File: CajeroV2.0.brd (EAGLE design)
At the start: 105 x 69 mm, 45 parts, among them K2 G5LE, T2 2N2222, T3 2N3904

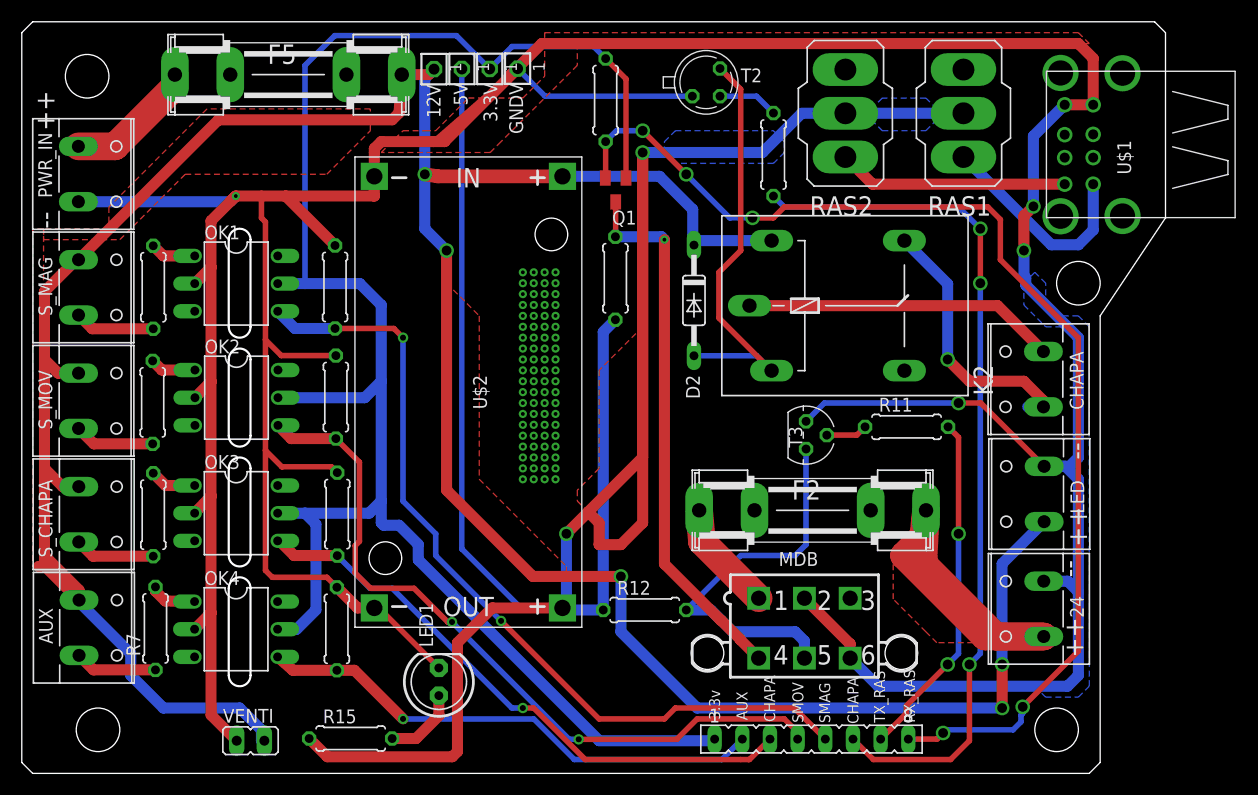
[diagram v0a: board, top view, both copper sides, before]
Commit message: V2.1
Cambio de posición un fusible y arreglo overlap
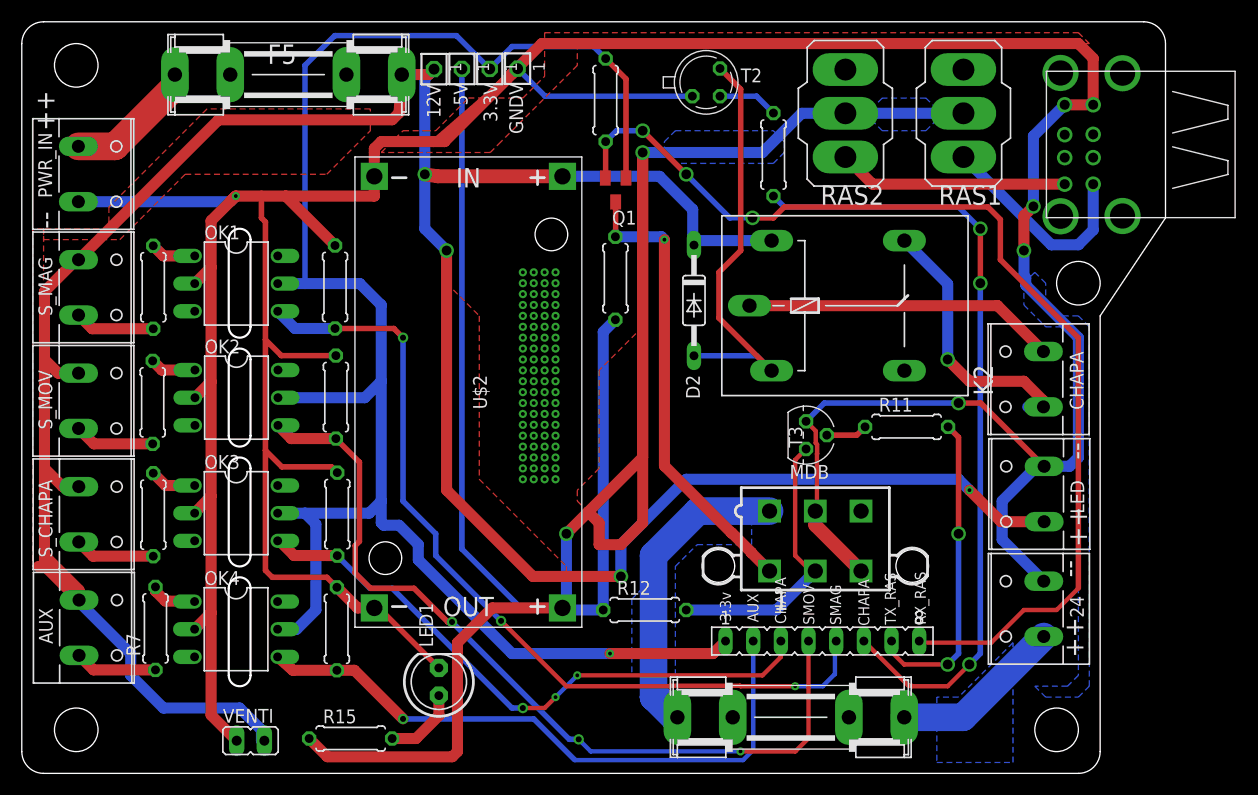
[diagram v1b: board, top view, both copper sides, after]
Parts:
- moved F2 19.1 mm to (70.6, 5.15)
- moved SV2 9.06 mm to (73.5, 12.1)
- moved MDB 8.06 mm to (72.8, 21.3)
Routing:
- net GND: track 397.3 -> 371.1 mm
- net 24VDC: track 39.5 -> 15.9 mm
- net N$21: track 10.2 -> 31.1 mm
- net +12V: track 275.6 -> 259.8 mm, vias 5 -> 4
- net ENTRADA_AUX: track 47.3 -> 57.9 mm
- net MASTER_TRANSMIT: track 35.9 -> 26.0 mm
- net SENSORMOV: track 68.1 -> 77.0 mm, vias 2 -> 3
- net RX_RASPBERRY: track 106.5 -> 97.8 mm, vias 5 -> 3
- net MASTER_RECEIVE: track 49.8 -> 42.3 mm
- net CHAPA: track 79.8 -> 72.9 mm
- net TX_RASPBERRY: track 32.0 -> 29.3 mm
- net +3V3: track 166.8 -> 164.9 mm, vias 0 -> 1
- net SENSORCHAPA: track 54.3 -> 55.9 mm, vias 1 -> 3
- net SENSORMAG: track 77.3 -> 78.9 mm, vias 2 -> 3
- added copper zone on layer 16, net 24VDC
- added copper zone on layer 16, net N$21
- removed copper zone on layer 1, net 24VDC
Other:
- outline, holes or cut-outs redrawn
- board text removed: "2"
- board text removed: "3"
- board text removed: "4"
- board text removed: "5"
- board text removed: "6"
